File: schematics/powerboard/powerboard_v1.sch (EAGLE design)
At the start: 18 parts, among them IC1 ACS756LCB-100B-PFF-T, IC2 AD2302ARDZ-5

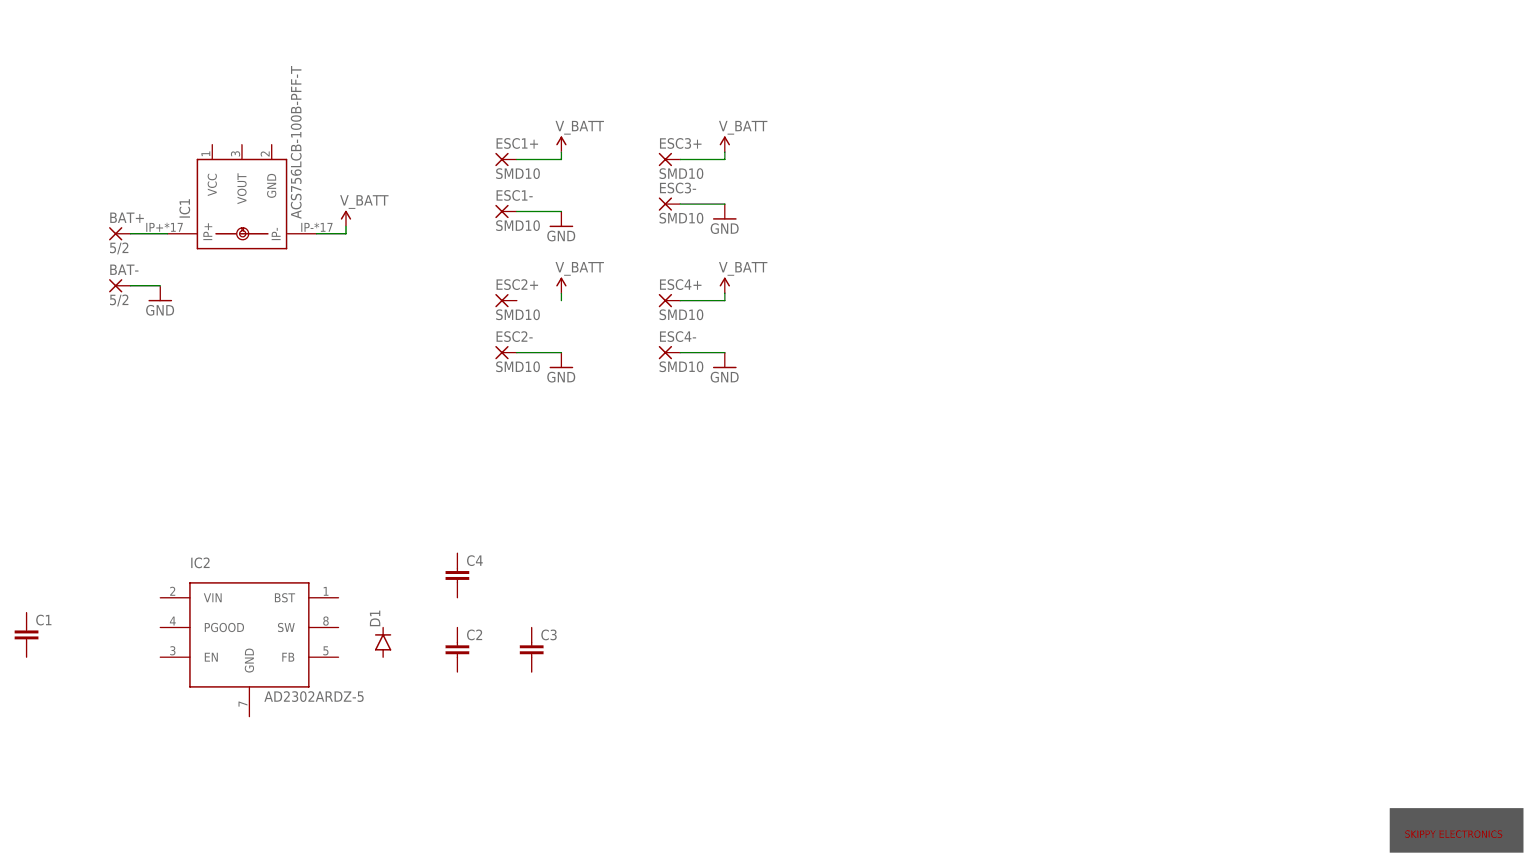
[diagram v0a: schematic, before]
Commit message: Inductor lib and powerboard 5V rail
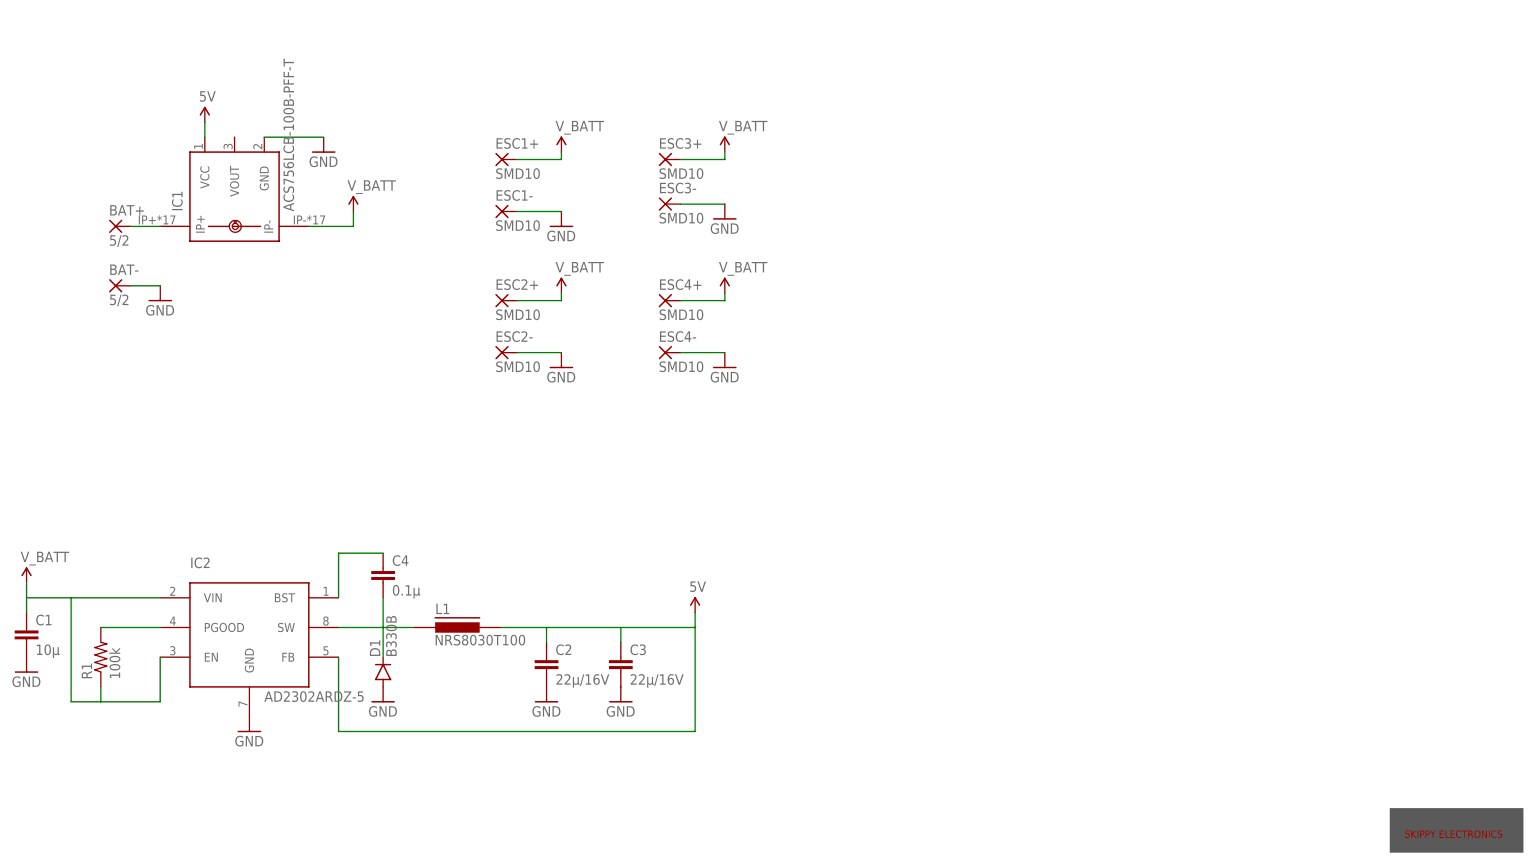
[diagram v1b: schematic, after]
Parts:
- added L1: NRS8030T100, inductors:NRS8030T100
- added R1: 100k, SparkFun-Passives:RESISTOR1206
- C1: value (none) -> 10µ
- C2, C3: value (none) -> 22µ/16V
- C4: value (none) -> 0.1µ
- D1: value (none) -> B330B
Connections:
- new net 5V: C2.1, C3.1, IC1.VCC, IC2.FB, L1.2
- new net N$2: C4.2, D1.C, IC2.SW, L1.1
- new net N$5: C4.1, IC2.BST
- new net N$6: IC2.PGOOD, R1.2
- net GND: now also C1.2, C2.2, C3.2, D1.A, IC1.GND, IC2.GND
- net V_BATT: now also C1.1, ESC2+.P, IC2.EN, IC2.VIN, R1.1
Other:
- moved on the sheet: BAT+, C2, C3, C4, D1, IC1
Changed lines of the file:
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@@
 <setting verticaltext="up"/>
 </settings>
-<grid distance="0.1" unitdist="inch" unit="inch" style="lines" multiple="1" display="no" altdistance="0.01" altunitdist="inch" altunit="inch"/>
+<grid distance="0.1" unitdist="inch" unit="inch" style="dots" multiple="1" display="yes" altdistance="0.01" altunitdist="inch" altunit="inch"/>
 <layers>
 <layer number="1" name="Top" color="4" fill="1" visible="no" active="no"/>
@@
 <part name="IC1" library="allegro" deviceset="ACS756" device="" technology="LCB-100B-PFF-T"/>
 <part name="IC2" library="dcdcconv" deviceset="AD2302ARDZ-5" device=""/>
-<part name="C1" library="SparkFun-Capacitors" deviceset="CAP" device="1206"/>
-<part name="C2" library="SparkFun-Capacitors" deviceset="CAP" device="1206"/>
-<part name="C3" library="SparkFun-Capacitors" deviceset="CAP" device="1206"/>
-<part name="C4" library="SparkFun-Capacitors" deviceset="CAP" device="1206"/>
-<part name="D1" library="SparkFun-DiscreteSemi" deviceset="DIODE" device="SMB"/>
+<part name="C1" library="SparkFun-Capacitors" deviceset="CAP" device="1206" value="10µ"/>
+<part name="C2" library="SparkFun-Capacitors" deviceset="CAP" device="1206" value="22µ/16V"/>
+<part name="C3" library="SparkFun-Capacitors" deviceset="CAP" device="1206" value="22µ/16V"/>
+<part name="C4" library="SparkFun-Capacitors" deviceset="CAP" device="1206" value="0.1µ"/>
+<part name="D1" library="SparkFun-DiscreteSemi" deviceset="DIODE" device="SMB" value="B330B"/>
+<part name="L1" library="inductors" deviceset="NRS8030T100" device=""/>
+<part name="R1" library="SparkFun-Passives" deviceset="RESISTOR" device="1206" value="100k"/>
+<part name="GND6" library="SparkFun-Aesthetics" deviceset="GND" device=""/>
+<part name="GND7" library="SparkFun-Aesthetics" deviceset="GND" device=""/>
+<part name="GND8" library="SparkFun-Aesthetics" deviceset="GND" device=""/>
+<part name="GND9" library="SparkFun-Aesthetics" deviceset="GND" device=""/>
+<part name="GND10" library="SparkFun-Aesthetics" deviceset="GND" device=""/>
+<part name="SUPPLY6" library="SparkFun-Aesthetics" deviceset="V_BATT" device=""/>
+<part name="SUPPLY7" library="SparkFun-Aesthetics" deviceset="5V" device=""/>
+<part name="SUPPLY8" library="SparkFun-Aesthetics" deviceset="5V" device=""/>
+<part name="GND11" library="SparkFun-Aesthetics" deviceset="GND" device=""/>
 </parts>
 <sheets>
@@
 </instance>
 <instance part="PLC1" gate="G$1" x="261" y="25"/>
-<instance part="SUPPLY1" gate="G$1" x="69.85" y="129.54"/>
+<instance part="SUPPLY1" gate="G$1" x="71.12" y="132.08"/>
 <instance part="SUPPLY2" gate="G$1" x="106.68" y="142.24"/>
 <instance part="SUPPLY3" gate="G$1" x="106.68" y="118.11"/>
 <instance part="SUPPLY4" gate="G$1" x="134.62" y="142.24"/>
 <instance part="SUPPLY5" gate="G$1" x="134.62" y="118.11"/>
-<instance part="BAT+" gate="G$1" x="30.48" y="128.27"/>
+<instance part="BAT+" gate="G$1" x="30.48" y="129.54"/>
 <instance part="BAT-" gate="G$1" x="30.48" y="119.38"/>
 <instance part="GND1" gate="1" x="38.1" y="116.84"/>
@@
 <instance part="ESC4+" gate="1" x="124.46" y="116.84"/>
 <instance part="ESC4-" gate="1" x="124.46" y="107.95"/>
-<instance part="IC1" gate="G$1" x="52.07" y="133.35" rot="R90"/>
+<instance part="IC1" gate="G$1" x="50.8" y="134.62" rot="R90"/>
 <instance part="IC2" gate="G$1" x="53.34" y="58.42"/>
 <instance part="C1" gate="G$1" x="15.24" y="58.42"/>
-<instance part="C2" gate="G$1" x="88.9" y="55.88"/>
-<instance part="C3" gate="G$1" x="101.6" y="55.88"/>
-<instance part="C4" gate="G$1" x="88.9" y="68.58"/>
-<instance part="D1" gate="G$1" x="76.2" y="58.42" rot="R90"/>
+<instance part="C2" gate="G$1" x="104.14" y="53.34"/>
+<instance part="C3" gate="G$1" x="116.84" y="53.34"/>
+<instance part="C4" gate="G$1" x="76.2" y="68.58"/>
+<instance part="D1" gate="G$1" x="76.2" y="53.34" rot="R90"/>
+<instance part="L1" gate="G$1" x="88.9" y="60.96"/>
+<instance part="R1" gate="G$1" x="27.94" y="55.88" rot="R90"/>
+<instance part="GND6" gate="1" x="53.34" y="43.18"/>
+<instance part="GND7" gate="1" x="76.2" y="48.26"/>
+<instance part="GND8" gate="1" x="104.14" y="48.26"/>
+<instance part="GND9" gate="1" x="116.84" y="48.26"/>
+<instance part="GND10" gate="1" x="15.24" y="53.34"/>
+<instance part="SUPPLY6" gate="G$1" x="15.24" y="68.58"/>
+<instance part="SUPPLY7" gate="G$1" x="129.54" y="63.5"/>
+<instance part="SUPPLY8" gate="G$1" x="45.72" y="147.32"/>
+<instance part="GND11" gate="1" x="66.04" y="142.24"/>
 </instances>
 <busses>
@@
 <pinref part="SUPPLY3" gate="G$1" pin="V_BATT"/>
 <wire x1="106.68" y1="118.11" x2="106.68" y2="116.84" width="0.1524" layer="91"/>
+<pinref part="ESC2+" gate="1" pin="P"/>
+<wire x1="99.06" y1="116.84" x2="106.68" y2="116.84" width="0.1524" layer="91"/>
+</segment>
+<segment>
+<pinref part="IC2" gate="G$1" pin="VIN"/>
+<pinref part="C1" gate="G$1" pin="1"/>
+<wire x1="38.1" y1="66.04" x2="22.86" y2="66.04" width="0.1524" layer="91"/>
+<wire x1="22.86" y1="66.04" x2="15.24" y2="66.04" width="0.1524" layer="91"/>
+<wire x1="15.24" y1="66.04" x2="15.24" y2="63.5" width="0.1524" layer="91"/>
+<wire x1="22.86" y1="48.26" x2="22.86" y2="66.04" width="0.1524" layer="91"/>
+<pinref part="R1" gate="G$1" pin="1"/>
+<wire x1="22.86" y1="48.26" x2="27.94" y2="48.26" width="0.1524" layer="91"/>
+<wire x1="27.94" y1="50.8" x2="27.94" y2="48.26" width="0.1524" layer="91"/>
+<pinref part="IC2" gate="G$1" pin="EN"/>
+<wire x1="38.1" y1="48.26" x2="38.1" y2="55.88" width="0.1524" layer="91"/>
+<wire x1="27.94" y1="48.26" x2="38.1" y2="48.26" width="0.1524" layer="91"/>
+<pinref part="SUPPLY6" gate="G$1" pin="V_BATT"/>
+<wire x1="15.24" y1="68.58" x2="15.24" y2="66.04" width="0.1524" layer="91"/>
 </segment>
 <segment>
 <pinref part="IC1" gate="G$1" pin="IP-"/>
-<wire x1="64.77" y1="128.27" x2="69.85" y2="128.27" width="0.1524" layer="91"/>
 <pinref part="SUPPLY1" gate="G$1" pin="V_BATT"/>
-<wire x1="69.85" y1="128.27" x2="69.85" y2="129.54" width="0.1524" layer="91"/>
+<wire x1="63.5" y1="129.54" x2="71.12" y2="129.54" width="0.1524" layer="91"/>
+<wire x1="71.12" y1="129.54" x2="71.12" y2="132.08" width="0.1524" layer="91"/>
 </segment>
 </net>
@@
 <wire x1="106.68" y1="107.95" x2="99.06" y2="107.95" width="0.1524" layer="91"/>
 </segment>
+<segment>
+<pinref part="D1" gate="G$1" pin="A"/>
+<pinref part="GND7" gate="1" pin="GND"/>
+</segment>
+<segment>
+<pinref part="C2" gate="G$1" pin="2"/>
+<pinref part="GND8" gate="1" pin="GND"/>
+</segment>
+<segment>
+<pinref part="C3" gate="G$1" pin="2"/>
+<pinref part="GND9" gate="1" pin="GND"/>
+</segment>
+<segment>
+<pinref part="IC2" gate="G$1" pin="GND"/>
+<pinref part="GND6" gate="1" pin="GND"/>
+</segment>
+<segment>
+<pinref part="C1" gate="G$1" pin="2"/>
+<pinref part="GND10" gate="1" pin="GND"/>
+</segment>
+<segment>
+<pinref part="GND11" gate="1" pin="GND"/>
+<wire x1="66.04" y1="144.78" x2="55.88" y2="144.78" width="0.1524" layer="91"/>
+<pinref part="IC1" gate="G$1" pin="GND"/>
+</segment>
 </net>
 <net name="N$1" class="0">
@@
 <pinref part="BAT+" gate="G$1" pin="P"/>
 <pinref part="IC1" gate="G$1" pin="IP+"/>
-<wire x1="33.02" y1="128.27" x2="39.37" y2="128.27" width="0.1524" layer="91"/>
-</segment>
-</net>
+<wire x1="33.02" y1="129.54" x2="38.1" y2="129.54" width="0.1524" layer="91"/>
+</segment>
+</net>
+<net name="N$2" class="0">
+<segment>
+<pinref part="C4" gate="G$1" pin="2"/>
+<wire x1="76.2" y1="66.04" x2="76.2" y2="60.96" width="0.1524" layer="91"/>
+<pinref part="IC2" gate="G$1" pin="SW"/>
+<wire x1="76.2" y1="60.96" x2="68.58" y2="60.96" width="0.1524" layer="91"/>
+<pinref part="L1" gate="G$1" pin="1"/>
+<wire x1="76.2" y1="60.96" x2="81.28" y2="60.96" width="0.1524" layer="91"/>
+<pinref part="D1" gate="G$1" pin="C"/>
+<wire x1="76.2" y1="60.96" x2="76.2" y2="55.88" width="0.1524" layer="91"/>
+</segment>
+</net>
+<net name="N$5" class="0">
+<segment>
+<pinref part="IC2" gate="G$1" pin="BST"/>
+<wire x1="68.58" y1="66.04" x2="68.58" y2="73.66" width="0.1524" layer="91"/>
+<pinref part="C4" gate="G$1" pin="1"/>
+<wire x1="68.58" y1="73.66" x2="76.2" y2="73.66" width="0.1524" layer="91"/>
+</segment>
+</net>
+<net name="N$6" class="0">
+<segment>
+<pinref part="IC2" gate="G$1" pin="PGOOD"/>
+<pinref part="R1" gate="G$1" pin="2"/>
+<wire x1="38.1" y1="60.96" x2="27.94" y2="60.96" width="0.1524" layer="91"/>
+</segment>
+</net>
+<net name="5V" class="0">
+<segment>
+<pinref part="L1" gate="G$1" pin="2"/>
+<pinref part="C2" gate="G$1" pin="1"/>
+<wire x1="96.52" y1="60.96" x2="104.14" y2="60.96" width="0.1524" layer="91"/>
+<wire x1="104.14" y1="60.96" x2="104.14" y2="58.42" width="0.1524" layer="91"/>
+<pinref part="C3" gate="G$1" pin="1"/>
+<wire x1="104.14" y1="60.96" x2="116.84" y2="60.96" width="0.1524" layer="91"/>
+<wire x1="116.84" y1="60.96" x2="116.84" y2="58.42" width="0.1524" layer="91"/>
+<pinref part="IC2" gate="G$1" pin="FB"/>
+<wire x1="68.58" y1="55.88" x2="68.58" y2="43.18" width="0.1524" layer="91"/>
+<wire x1="68.58" y1="43.18" x2="129.54" y2="43.18" width="0.1524" layer="91"/>
+<wire x1="129.54" y1="43.18" x2="129.54" y2="60.96" width="0.1524" layer="91"/>
+<wire x1="129.54" y1="60.96" x2="116.84" y2="60.96" width="0.1524" layer="91"/>
+<pinref part="SUPPLY7" gate="G$1" pin="5V"/>
+<wire x1="129.54" y1="63.5" x2="129.54" y2="60.96" width="0.1524" layer="91"/>
+</segment>
+<segment>
+<pinref part="SUPPLY8" gate="G$1" pin="5V"/>
+<pinref part="IC1" gate="G$1" pin="VCC"/>
+<wire x1="45.72" y1="147.32" x2="45.72" y2="144.78" width="0.1524" layer="91"/>
+</segment>
+</net>

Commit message: Power board finalized
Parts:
- added JP1: JTAG_CONNPTH, connectors:JTAG_CONNPTH
- added JP2: M02LOCK, SparkFun-Connectors:M02LOCK
- added LED1, LED2, LED3: RED, eagle-ltspice:LED_E
- added R2, R3, R4: 100k, SparkFun-Passives:RESISTOR1206
- added R5, R7: 10k, SparkFun-Passives:RESISTOR1206
- added R6: 1M, SparkFun-Passives:RESISTOR1206
- added R8: 50k, SparkFun-Passives:RESISTOR1206
- added U$1: AD2302ARDZ-3.3, dcdcconv:AD2302ARDZ-3.3
- added Y1: 10MHZ, SparkFun-FreqCtrl:RESONATOR8MHZ
- IC2: value AD2302ARDZ-5 -> ATMEGA644-A; device dcdcconv:AD2302ARDZ-5 -> atmega:ATMEGA644-A
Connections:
- new net 3.3V: C2.1, C3.1, IC2.AVCC, IC2.VCC, IC2.VCC1, IC2.VCC2, JP1.VCC, L1.2, R3.1, R5.2, U$1.FB
- new net LO_BATT_LED: IC2.(ADC7)PA7, R4.1
- new net N$10: IC2.(ADC0)PA0, R7.2, R8.1
- new net N$3: R1.1, U$1.PGOOD
- new net N$4: LED1.A, R2.2
- new net N$7: LED3.A, R4.2
- new net N$8: IC2.XTAL2, R6.2, Y1.1
- new net N$9: IC2.XTAL1, R6.1, Y1.3
- new net NSRST: IC2.RESET, JP1.NSRRST, R5.1
- new net SCL: IC2.PC0(SCL), JP2.2
- new net SDA: IC2.PC1(SDA), JP2.1
- new net TCK: IC2.(TCK)PC2, JP1.TCK
- new net TDI: IC2.(TDI)PC5, JP1.TDI
- new net TDO: IC2.(TDO)PC4, JP1.TDO
- new net TMS: IC2.(TMS)PC3, JP1.TMS
- net 5V: no longer C2.1, C3.1, IC2.FB, L1.2
- net GND: now also IC2.AGND, IC2.GND1, IC2.GND2, JP1.GND, LED1.C, LED2.C, LED3.C, R7.1, U$1.GND, Y1.2
- net N$2: now also U$1.SW; no longer IC2.SW
- net N$5: now also U$1.BST; no longer IC2.BST
- net N$6: now also LED2.A, R3.2; no longer IC2.PGOOD, R1.2
- net V_BATT: now also R1.2, R2.1, R8.2, U$1.EN, U$1.VIN; no longer IC2.EN, IC2.VIN, R1.1
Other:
- moved on the sheet: ESC1+, ESC2-, ESC3+, ESC4-, R1
